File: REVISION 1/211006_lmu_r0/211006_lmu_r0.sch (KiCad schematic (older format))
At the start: 2 parts

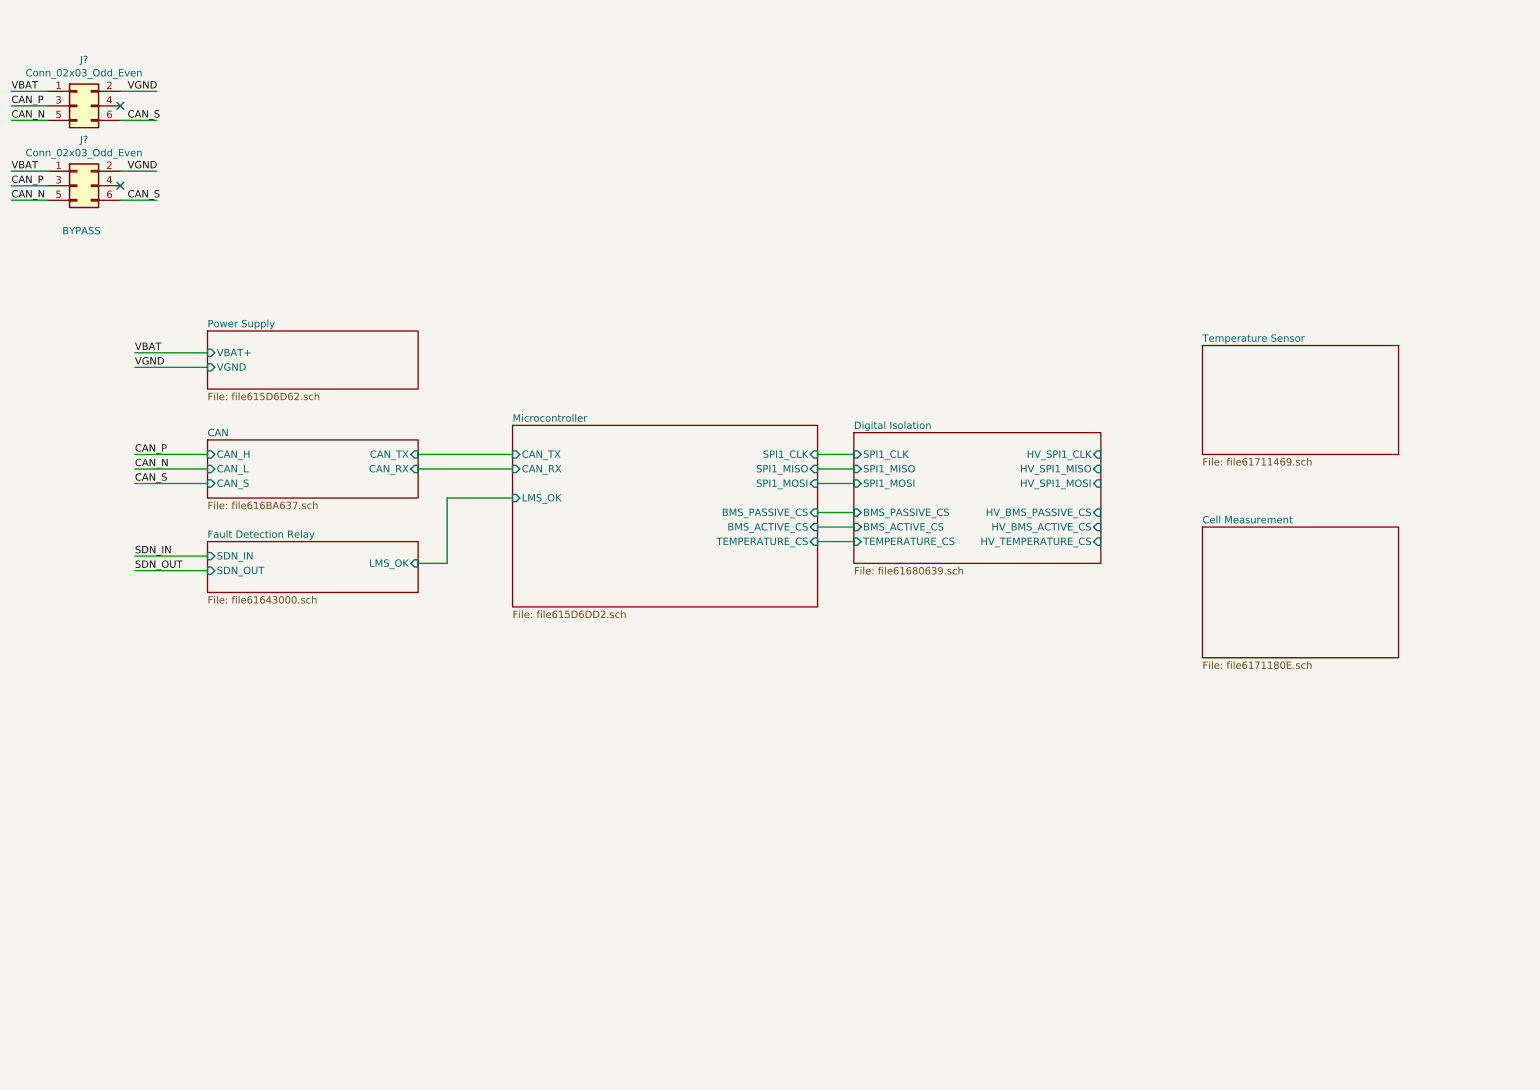
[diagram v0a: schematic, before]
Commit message: Added new a-balancer interface
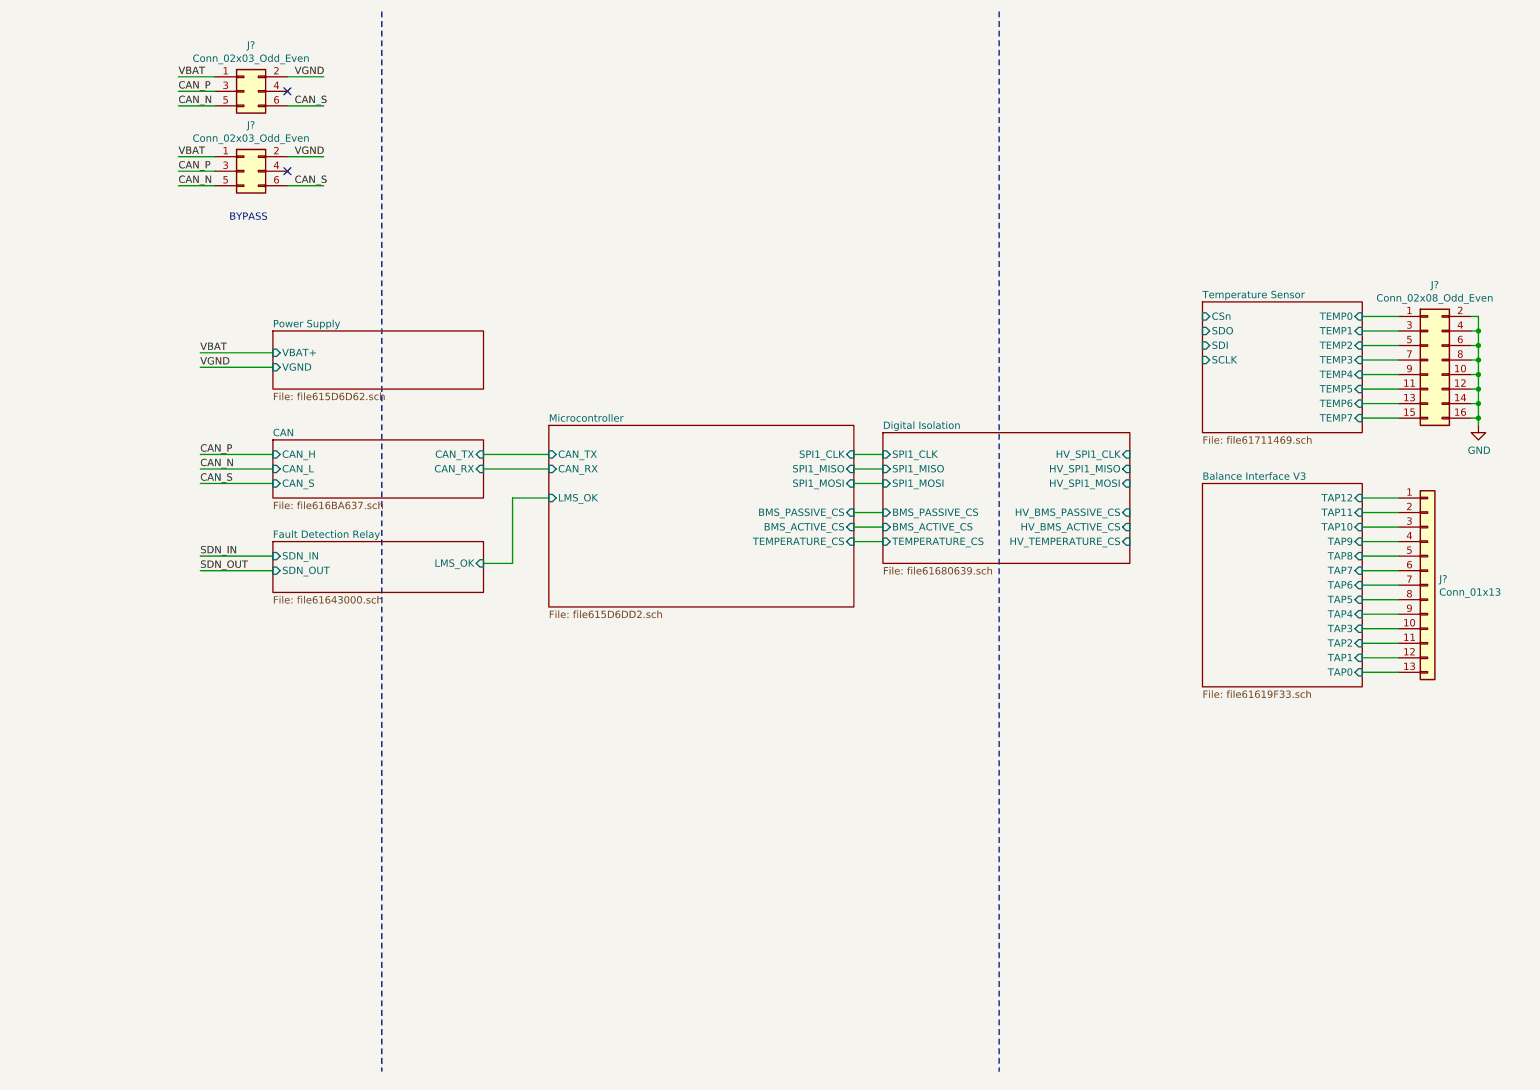
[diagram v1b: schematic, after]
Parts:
- added J?: Conn_01x13, symbol Connector_Generic:Conn_01x13
- added J?: Conn_02x08_Odd_Even, symbol Connector_Generic:Conn_02x08_Odd_Even
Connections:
- net labels added: GND
- wire segments 28 -> 65
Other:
- moved on the sheet: J?

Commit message: LMU design init
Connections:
- net labels added: GND_ISO
- net labels removed: GND
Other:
- moved on the sheet: J?
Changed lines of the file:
@@
-$EndSheet
-$Sheet
-S 2500 4050 1450 350
-U 61643001
-F0 "Fault Detection Relay" 50
-F1 "file61643000.sch" 50
-F2 "LMS_OK" I R 3950 4200 50
-F3 "SDN_IN" I L 2500 4150 50
-F4 "SDN_OUT" I L 2500 4250 50
 $EndSheet
 $Sheet
@@
 	4400 3550 3950 3550
 Wire Wire Line
-	3950 4200 4150 4200
-Wire Wire Line
 	4150 4200 4150 3750
 Wire Wire Line
 	4150 3750 4400 3750
-Text Label 2000 4150 0    50   ~ 0
-SDN_IN
-Text Label 2000 4250 0    50   ~ 0
-SDN_OUT
 Text Label 2000 3450 0    50   ~ 0
 CAN_P
@@
 L Connector_Generic:Conn_02x03_Odd_Even J?
 U 1 1 616F9826
-P 2300 950
-F 0 "J?" H 2350 1267 50  0000 C CNN
-F 1 "Conn_02x03_Odd_Even" H 2350 1176 50  0000 C CNN
-F 2 "" H 2300 950 50  0001 C CNN
-F 3 "~" H 2300 950 50  0001 C CNN
-	1    2300 950
-	1    0    0    -1
-$EndComp
-Text Notes 2200 1850 0    50   ~ 0
+P 1800 1200
+F 0 "J?" H 1850 1517 50  0000 C CNN
+F 1 "Conn_02x03_Odd_Even" H 1850 1426 50  0000 C CNN
+F 2 "" H 1800 1200 50  0001 C CNN
+F 3 "~" H 1800 1200 50  0001 C CNN
+	1    1800 1200
+	1    0    0    -1
+$EndComp
+Text Notes 1700 2100 0    50   ~ 0
 BYPASS
-Text Label 1850 850  0    50   ~ 0
+Text Label 1350 1100 0    50   ~ 0
 VBAT
-Text Label 2650 850  0    50   ~ 0
+Text Label 2150 1100 0    50   ~ 0
 VGND
-Text Label 1850 950  0    50   ~ 0
+Text Label 1350 1200 0    50   ~ 0
 CAN_P
-Text Label 1850 1050 0    50   ~ 0
+Text Label 1350 1300 0    50   ~ 0
 CAN_N
-Wire Wire Line
-	2000 4150 2500 4150
-Wire Wire Line
-	2500 4250 2000 4250
 Wire Wire Line
 	2500 3450 2000 3450
@@
 Wire Wire Line
 	2000 3650 2500 3650
-Text Label 2650 1050 0    50   ~ 0
+Text Label 2150 1300 0    50   ~ 0
 CAN_S
 Wire Wire Line
-	2600 1050 2850 1050
-NoConn ~ 2600 950
-Wire Wire Line
-	2600 850  2850 850
-Wire Wire Line
-	2100 850  1850 850
-Wire Wire Line
-	1850 950  2100 950
-Wire Wire Line
-	2100 1050 1850 1050
+	2100 1300 2350 1300
+NoConn ~ 2100 1200
+Wire Wire Line
+	2100 1100 2350 1100
+Wire Wire Line
+	1600 1100 1350 1100
+Wire Wire Line
+	1350 1200 1600 1200
+Wire Wire Line
+	1600 1300 1350 1300
 $Comp
 L Connector_Generic:Conn_02x03_Odd_Even J?
 U 1 1 6170BFBA
-P 2300 1500
-F 0 "J?" H 2350 1817 50  0000 C CNN
-F 1 "Conn_02x03_Odd_Even" H 2350 1726 50  0000 C CNN
-F 2 "" H 2300 1500 50  0001 C CNN
-F 3 "~" H 2300 1500 50  0001 C CNN
-	1    2300 1500
-	1    0    0    -1
-$EndComp
-Text Label 1850 1400 0    50   ~ 0
+P 1800 1750
+F 0 "J?" H 1850 2067 50  0000 C CNN
+F 1 "Conn_02x03_Odd_Even" H 1850 1976 50  0000 C CNN
+F 2 "" H 1800 1750 50  0001 C CNN
+F 3 "~" H 1800 1750 50  0001 C CNN
+	1    1800 1750
+	1    0    0    -1
+$EndComp
+Text Label 1350 1650 0    50   ~ 0
 VBAT
-Text Label 2650 1400 0    50   ~ 0
+Text Label 2150 1650 0    50   ~ 0
 VGND
-Text Label 1850 1500 0    50   ~ 0
+Text Label 1350 1750 0    50   ~ 0
 CAN_P
-Text Label 1850 1600 0    50   ~ 0
+Text Label 1350 1850 0    50   ~ 0
 CAN_N
-Text Label 2650 1600 0    50   ~ 0
+Text Label 2150 1850 0    50   ~ 0
 CAN_S
 Wire Wire Line
-	2600 1600 2850 1600
-NoConn ~ 2600 1500
-Wire Wire Line
-	2600 1400 2850 1400
-Wire Wire Line
-	2100 1400 1850 1400
-Wire Wire Line
-	1850 1500 2100 1500
-Wire Wire Line
-	2100 1600 1850 1600
+	2100 1850 2350 1850
+NoConn ~ 2100 1750
+Wire Wire Line
+	2100 1650 2350 1650
+Wire Wire Line
+	1600 1650 1350 1650
+Wire Wire Line
+	1350 1750 1600 1750
+Wire Wire Line
+	1600 1850 1350 1850
 $Sheet
 S 8900 2400 1100 900
@@
 	1    0    0    -1
 $EndComp
-$Comp
-L power:GND #PWR?
-U 1 1 617103E5
+Wire Wire Line
+	10250 3200 10000 3200
+Wire Wire Line
+	10000 3100 10250 3100
+Wire Wire Line
+	10250 3000 10000 3000
+Wire Wire Line
+	10000 2900 10250 2900
+Wire Wire Line
+	10250 2800 10000 2800
+Wire Wire Line
+	10000 2700 10250 2700
+Wire Wire Line
+	10250 2600 10000 2600
+Wire Wire Line
+	10000 2500 10250 2500
+Wire Wire Line
+	10750 2500 10800 2500
+Wire Wire Line
+	10800 2500 10800 2600
+Wire Wire Line
+	10750 3200 10800 3200
+Connection ~ 10800 3200
+Wire Wire Line
+	10800 3200 10800 3250
+Wire Wire Line
+	10750 3100 10800 3100
+Connection ~ 10800 3100
+Wire Wire Line
+	10800 3100 10800 3200
+Wire Wire Line
+	10750 3000 10800 3000
+Connection ~ 10800 3000
+Wire Wire Line
+	10800 3000 10800 3100
+Wire Wire Line
+	10750 2900 10800 2900
+Connection ~ 10800 2900
+Wire Wire Line
+	10800 2900 10800 3000
+Wire Wire Line
+	10750 2800 10800 2800
+Connection ~ 10800 2800
+Wire Wire Line
+	10800 2800 10800 2900
+Wire Wire Line
+	10750 2700 10800 2700
+Connection ~ 10800 2700
+Wire Wire Line
+	10800 2700 10800 2800
+Wire Wire Line
+	10750 2600 10800 2600
+Connection ~ 10800 2600
+Wire Wire Line
+	10800 2600 10800 2700
+Wire Wire Line
+	2500 4250 2000 4250
+Wire Wire Line
+	2000 4150 2500 4150
+Text Label 2000 4250 0    50   ~ 0
+SDN_OUT
+Text Label 2000 4150 0    50   ~ 0
+SDN_IN
+$Sheet
+S 2500 4050 1450 350
+U 61643001
+F0 "Fault Detection Relay" 50
+F1 "file61643000.sch" 50
+F2 "LMS_OK" I R 3950 4200 50
+F3 "SDN_IN" I L 2500 4150 50
+F4 "SDN_OUT" I L 2500 4250 50
+$EndSheet
+Wire Wire Line
+	3950 4200 4150 4200
+$Comp
+L gnd_iso:GND_ISO #PWR?
+U 1 1 61694729
 P 10800 3250
 F 0 "#PWR?" H 10800 3000 50  0001 C CNN
-F 1 "GND" H 10805 3077 50  0000 C CNN
+F 1 "GND_ISO" H 10805 3077 50  0000 C CNN
 F 2 "" H 10800 3250 50  0001 C CNN
 F 3 "" H 10800 3250 50  0001 C CNN
@@
 	1    0    0    -1
 $EndComp
-Wire Wire Line
-	10250 3200 10000 3200
-Wire Wire Line
-	10000 3100 10250 3100
-Wire Wire Line
-	10250 3000 10000 3000
-Wire Wire Line
-	10000 2900 10250 2900
-Wire Wire Line
-	10250 2800 10000 2800
-Wire Wire Line
-	10000 2700 10250 2700
-Wire Wire Line
-	10250 2600 10000 2600
-Wire Wire Line
-	10000 2500 10250 2500
-Wire Wire Line
-	10750 2500 10800 2500
-Wire Wire Line
-	10800 2500 10800 2600
-Wire Wire Line
-	10750 3200 10800 3200
-Connection ~ 10800 3200
-Wire Wire Line
-	10800 3200 10800 3250
-Wire Wire Line
-	10750 3100 10800 3100
-Connection ~ 10800 3100
-Wire Wire Line
-	10800 3100 10800 3200
-Wire Wire Line
-	10750 3000 10800 3000
-Connection ~ 10800 3000
-Wire Wire Line
-	10800 3000 10800 3100
-Wire Wire Line
-	10750 2900 10800 2900
-Connection ~ 10800 2900
-Wire Wire Line
-	10800 2900 10800 3000
-Wire Wire Line
-	10750 2800 10800 2800
-Connection ~ 10800 2800
-Wire Wire Line
-	10800 2800 10800 2900
-Wire Wire Line
-	10750 2700 10800 2700
-Connection ~ 10800 2700
-Wire Wire Line
-	10800 2700 10800 2800
-Wire Wire Line
-	10750 2600 10800 2600
-Connection ~ 10800 2600
-Wire Wire Line
-	10800 2600 10800 2700
 $EndSCHEMATC

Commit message: Finished schematic, ready for pcb layout
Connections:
- net labels added: CS_ACTIVE_LOWER, CS_ACTIVE_UPPER, CS_PASSIVE, CS_TEMPERATURE, WDT_ACTIVE_LOWER, WDT_ACTIVE_UPPER, WDT_PASSIVE
- wire segments 65 -> 125
- no-connect marks 2 -> 6
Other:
- moved on the sheet: J?
